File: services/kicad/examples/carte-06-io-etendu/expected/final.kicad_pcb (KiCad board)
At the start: 2 copper layers, 80 x 60 mm, 35 parts, among them J1 IN_5V, J2 SWD, J3 IO0, J4 IO1, U1 STM32F103C8T6, U2 AMS1117-3.3

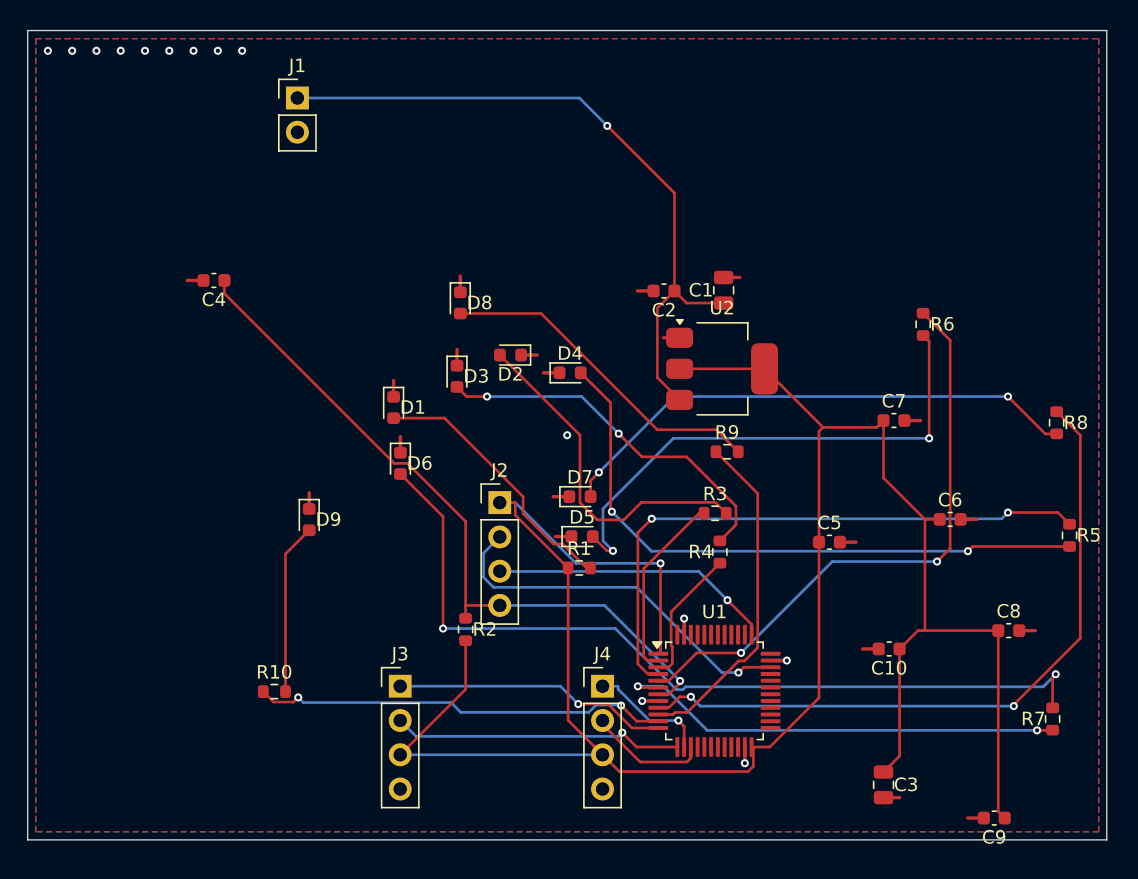
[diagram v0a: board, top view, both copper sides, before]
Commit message: feat(kicad): placement pro et routage 100 % fabricable sur les 16 cartes -- integration sur main (#164)
Branche d'integration coupee depuis origin/main (fab2a82, PR #162) : les
fichiers cles de main etaient des instantanes de feat/placement-seed-snap-
bypass (routing.py = 7981019, placement.py = 437a8b4...). On reprend donc
l'arbre entier de cette branche (345 commits, dernier 9f48667) et on y
conserve ce que main seul apportait :
- tools/verrou_routage.py + son test : « 6,2 Go par routage » rectifie
  (0,2 Go mesure ; c'est la concurrence qui emballe la memoire) ;
- tests/test_driver_llm_resync.py ;
- CLAUDE.md, PLAN.md, DECISIONS.md : fusion a trois voies, les sections
  des deux lignes conservees (2026-09-05 conteneur/verrou, 2026-09-07
  parcours asynchrone et chaine du driver, 2026-09-09/10 lecons).
Les skills *-delegate restent supprimes (remplaces le 2026-08-30).

Contenu : banc en deux phases (placement valide puis routage gele), snap
sur les regles natives, repli GND cible, journal Freerouting incremental,
horloge sans progres, via d'echappement vers le plan principal,
serigraphie degagee ; 16 cartes livrees a 100 %, 0 erreur DRC.

Verification : pytest services/kicad 1805 passed, 16 skipped ;
pnpm type-check 8/8.


Claude-Session: https://claude.ai/code/session_01TnMqm4La2CxQHHB5K8aSSV

Co-authored-by: Claude Fable 5.1 <noreply@anthropic.com>
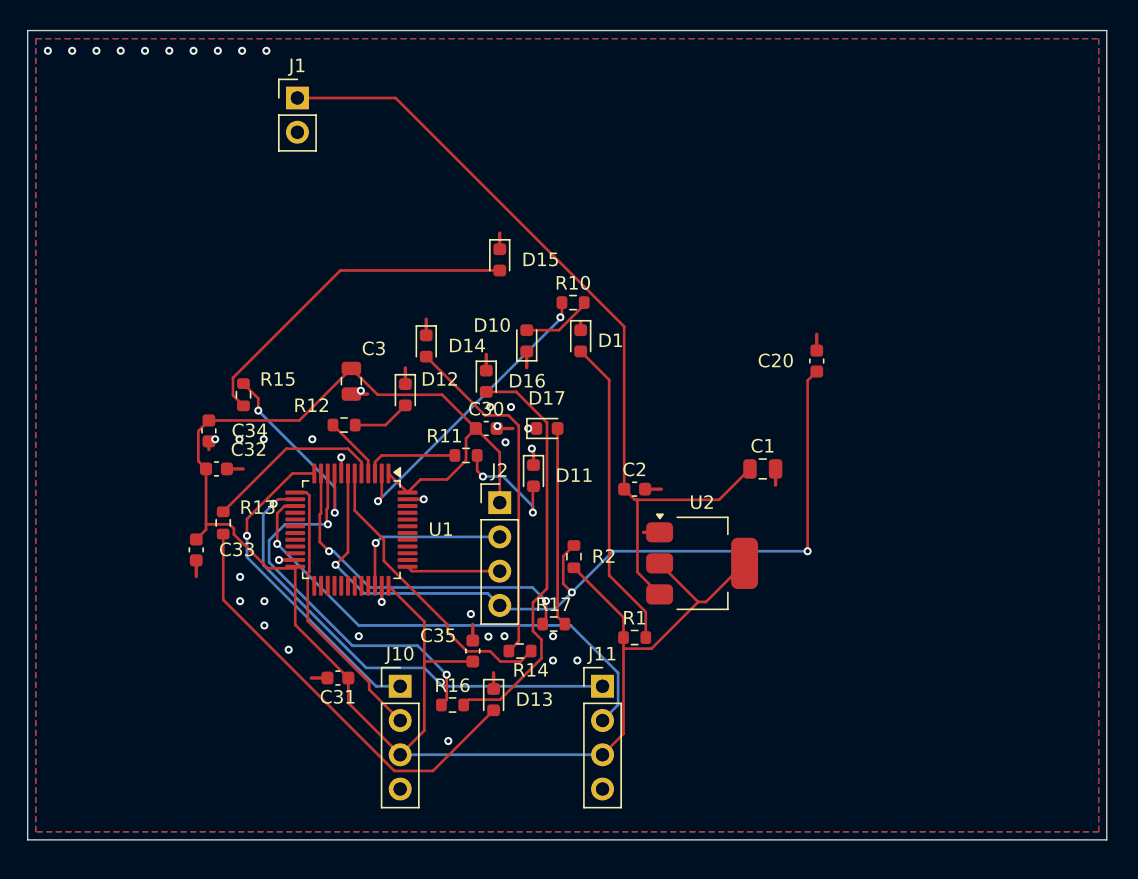
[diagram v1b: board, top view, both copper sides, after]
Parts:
- removed C10, C4, C5, C6, C7, C8, C9: 100nF, C_0603_1608Metric
- removed D2, D3, D4, D5, D6, D7, D8, D9: LED, LED_0603_1608Metric
- removed J3: IO0, PinHeader_1x04_P2.54mm_Vertical
- removed J4: IO1, PinHeader_1x04_P2.54mm_Vertical
- removed R3, R4, R5, R6, R7, R8, R9: 1k, R_0603_1608Metric
- added C20: 100nF, C_0603_1608Metric, F.Cu at (167.0, 99.5)
- added C30: 100nF, C_0603_1608Metric, F.Cu at (142.5, 104.5)
- added C31: 100nF, C_0603_1608Metric, F.Cu at (131.5, 123.0)
- added C32: 100nF, C_0603_1608Metric, F.Cu at (122.5, 107.5)
- added C33: 100nF, C_0603_1608Metric, F.Cu at (121.0, 113.5)
- added C34: 100nF, C_0603_1608Metric, F.Cu at (121.9, 104.7)
- added C35: 100nF, C_0603_1608Metric, F.Cu at (141.5, 121.0)
- added D10: LED, LED_0603_1608Metric, F.Cu at (145.5, 98.0)
- added D11: LED, LED_0603_1608Metric, F.Cu at (146.0, 108.0)
- added D12: LED, LED_0603_1608Metric, F.Cu at (136.5, 102.0)
- added D13: LED, LED_0603_1608Metric, F.Cu at (143.0, 124.6)
- added D14: LED, LED_0603_1608Metric, F.Cu at (138.0, 98.4)
- added D15: LED, LED_0603_1608Metric, F.Cu at (143.5, 92.0)
- added D16: LED, LED_0603_1608Metric, F.Cu at (142.5, 101.0)
- added D17: LED, LED_0603_1608Metric, F.Cu at (147.0, 104.5)
- added J10: IO0, PinHeader_1x04_P2.54mm_Vertical, F.Cu at (136.1, 123.6)
- added J11: IO1, PinHeader_1x04_P2.54mm_Vertical, F.Cu at (151.1, 123.6)
- added R11: 1k, R_0603_1608Metric, F.Cu at (141.0, 106.5)
- added R12: 1k, R_0603_1608Metric, F.Cu at (132.0, 104.2)
- added R13: 1k, R_0603_1608Metric, F.Cu at (123.0, 111.5)
- added R14: 1k, R_0603_1608Metric, F.Cu at (145.0, 121.0)
- added R15: 1k, R_0603_1608Metric, F.Cu at (124.5, 102.0)
- added R16: 1k, R_0603_1608Metric, F.Cu at (140.0, 125.0)
- added R17: 1k, R_0603_1608Metric, F.Cu at (147.5, 119.0)
- moved C3 49.5 mm to (132.5, 101.0)
- moved R10 36.4 mm to (148.9, 95.2)
- moved U1 29.5 mm to (132.5, 112.0), turned to -90 degrees
- moved C2 14.9 mm to (153.5, 109.0), turned to 0 degrees
- moved D1 14.7 mm to (149.5, 98.0)
- moved U2 14.5 mm to (158.5, 114.5)
- moved C1 13.6 mm to (163.0, 107.5), turned to 0 degrees
- moved R2 9.68 mm to (149.0, 114.0)
- moved R1 6.59 mm to (153.5, 120.0)
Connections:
- R10 pad 1: IO_L7 -> IO_L0
- R10 pad 2: LEDA7 -> LEDA0
- U1 pad 36: Net-(U1-36) -> +3V3
- U1 pad 48: Net-(U1-48) -> +3V3
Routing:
- net LEDA2: track 46.5 -> 4.32 mm, vias 2 -> 0
- net IO_L2: track 44.5 -> 4.67 mm, vias 2 -> 0
- net LEDA4: track 63.1 -> 26.0 mm, vias 2 -> 0
- net IO_L5: track 51.6 -> 15.3 mm
- net +3V3: track 175.2 -> 139.1 mm, vias 1 -> 0
- net IO_L3: track 44.0 -> 13.4 mm, vias 2 -> 0
- net EXT1_2: track 8.93 -> 37.1 mm, vias 0 -> 1
- net EXT1_1: track 8.94 -> 35.5 mm
- net LEDA0: track 25.6 -> 5.21 mm
- net LEDA1: track 27.4 -> 8.79 mm
- net SWDIO: track 27.9 -> 12.6 mm
- net SWCLK: track 21.1 -> 6.97 mm, vias 1 -> 0
- net LEDA5: track 39.5 -> 25.5 mm, vias 2 -> 0
- net IO_L4: track 33.7 -> 22.0 mm, vias 2 -> 0
- net VIN: track 51.4 -> 61.6 mm, vias 1 -> 0
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
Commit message: test(examples): quatre cartes livrées plus petites — contour resserré mesuré sur le banc (D-2026-09-13-c A)
Banc rejoué en taille heuristique (phase 1 puis phase 2 à placement gelé) :
carte-01 25x20 -> 24,8x17 (84 % de surface), carte-04 60x45 -> 45x44,8
(75 %), carte-06 80x60 -> 65,2x59,8 (81 %), carte-07 110x80 -> 99,5x79,8
(90 %) — toutes 100 % routées, 0 erreur DRC (vérifié en local), rendus 3D
régénérés. Gain nul sur les cartes denses (le génétique remplit la carte) ;
08 et 09 non livrées (dispersion du routage, surface inchangée) ; carte-11
non livrée (carte d'escalade). Tableau complet dans docs/DECISIONS.md.

Co-Authored-By: Claude Fable 5.1 <noreply@anthropic.com>
Claude-Session: https://claude.ai/code/session_01TnMqm4La2CxQHHB5K8aSSV
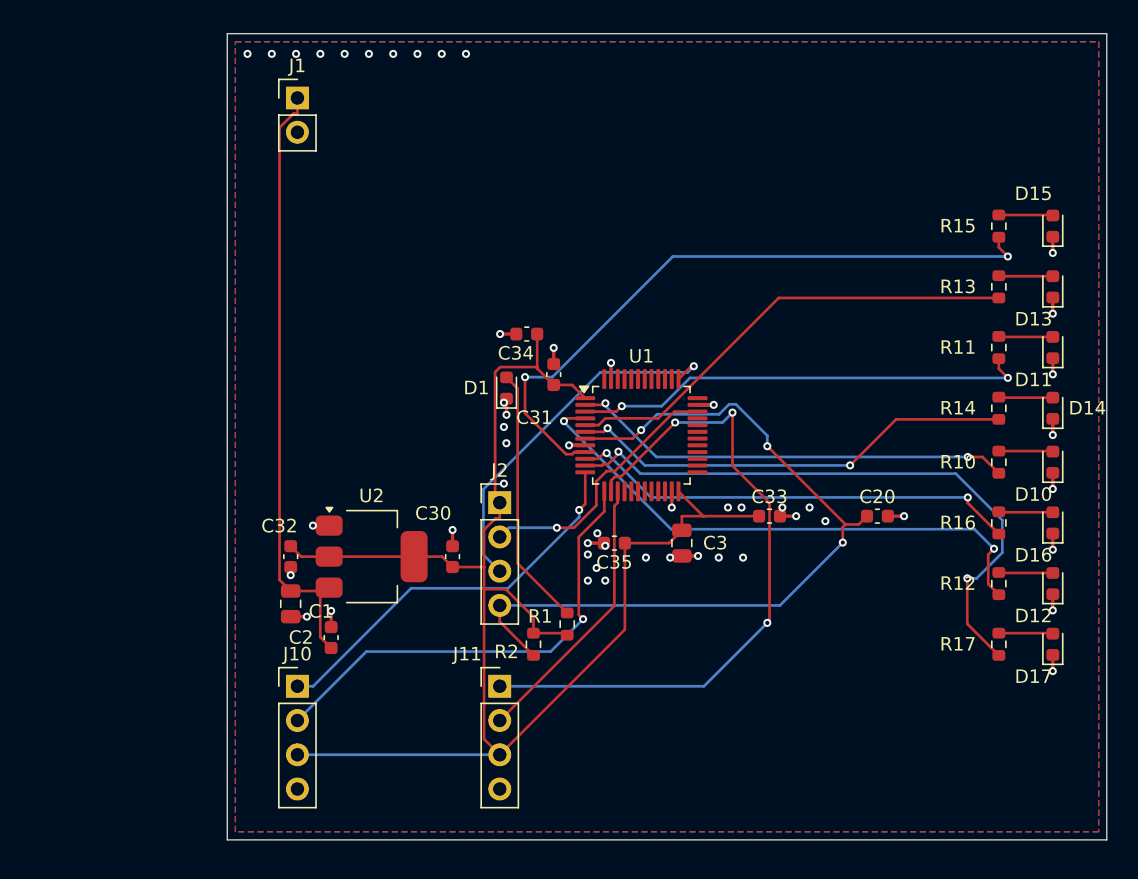
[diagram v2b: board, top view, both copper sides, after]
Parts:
- moved R13 60.1 mm to (180.5, 94.0), turned to 90 degrees
- moved R15 57.4 mm to (180.5, 89.5), turned to 90 degrees
- moved D13 51.5 mm to (184.5, 94.0), turned to 90 degrees
- moved D12 50.0 mm to (184.5, 116.0), turned to 90 degrees
- moved R12 49.9 mm to (180.5, 116.0), turned to 90 degrees
- moved D14 46.7 mm to (184.5, 103.0), turned to 90 degrees
- moved D16 43.3 mm to (184.5, 111.5), turned to 90 degrees
- moved R16 42.7 mm to (180.5, 111.5), turned to 90 degrees
- moved C33 42.6 mm to (163.5, 111.0), turned to 0 degrees
- moved D15 41.1 mm to (184.5, 89.5), turned to 90 degrees
- moved D17 40.8 mm to (184.5, 120.5), turned to 90 degrees
- moved R11 40.3 mm to (180.5, 98.5), turned to 90 degrees
- moved D10 40.0 mm to (184.5, 107.0)
- moved R14 39.8 mm to (180.5, 103.0), turned to 90 degrees
- moved D11 39.7 mm to (184.5, 98.5), turned to 90 degrees
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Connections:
- U1 pad 36: +3V3 -> Net-(U1-36)
- U1 pad 48: +3V3 -> Net-(U1-48)
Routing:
- net IO_L2: track 4.67 -> 41.4 mm, vias 0 -> 2
- net IO_L5: track 15.3 -> 49.7 mm
- net LEDA3: track 32.0 -> 4.02 mm
- net IO_L1: track 6.98 -> 34.1 mm, vias 0 -> 2
- net +3V3: track 139.1 -> 112.3 mm
- net LEDA6: track 30.8 -> 4.02 mm
- net LEDA4: track 26.0 -> 4.02 mm
- net LEDA5: track 25.5 -> 4.02 mm
- net IO_L3: track 13.4 -> 34.6 mm
- net SWCLK: track 6.97 -> 27.5 mm, vias 0 -> 1
- net IO_L7: track 25.5 -> 46.0 mm
- net VIN: track 61.6 -> 45.1 mm
- net EXT1_2: track 37.1 -> 20.6 mm, vias 1 -> 0
- net EXT1_1: track 35.5 -> 50.5 mm, vias 1 -> 3
- net EXT0_2: track 20.7 -> 34.7 mm, vias 0 -> 1
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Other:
- board size 80 x 60 mm -> 65.2 x 59.8 mm

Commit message: chore(banc): relivrer carte-01..10 avec la couture corrigee
Boards reroutes par HTTP depuis placement.kicad_pcb inchange, avec le
code de #217. Juges par remesurer_banc.py : 0 erreur, 0 connexion
manquante sur les dix. 678 -> 443 vias ; la rangee de vias GND du bord
haut a disparu.

mesures.json : `board` recompte, `drc_du_board` rejuge, nouvelle cle
`couture_corrigee` (date, vias_avant, couches). journal.txt et les
champs du run d origine sont laisses tels quels et le disent.
rendu-3d.png : kicad-cli, modeles 3D, iso 1400x900.

Couches d un tirage : huit cartes sur 2, carte-08 et carte-10 sur 4.
CLAUDE.md et BANC_DRIVER_LLM.md recomptes. carte-11 non touchee.

Co-Authored-By: Claude Opus 5 (1M context) <noreply@anthropic.com>
Claude-Session: https://claude.ai/code/session_01TnMqm4La2CxQHHB5K8aSSV
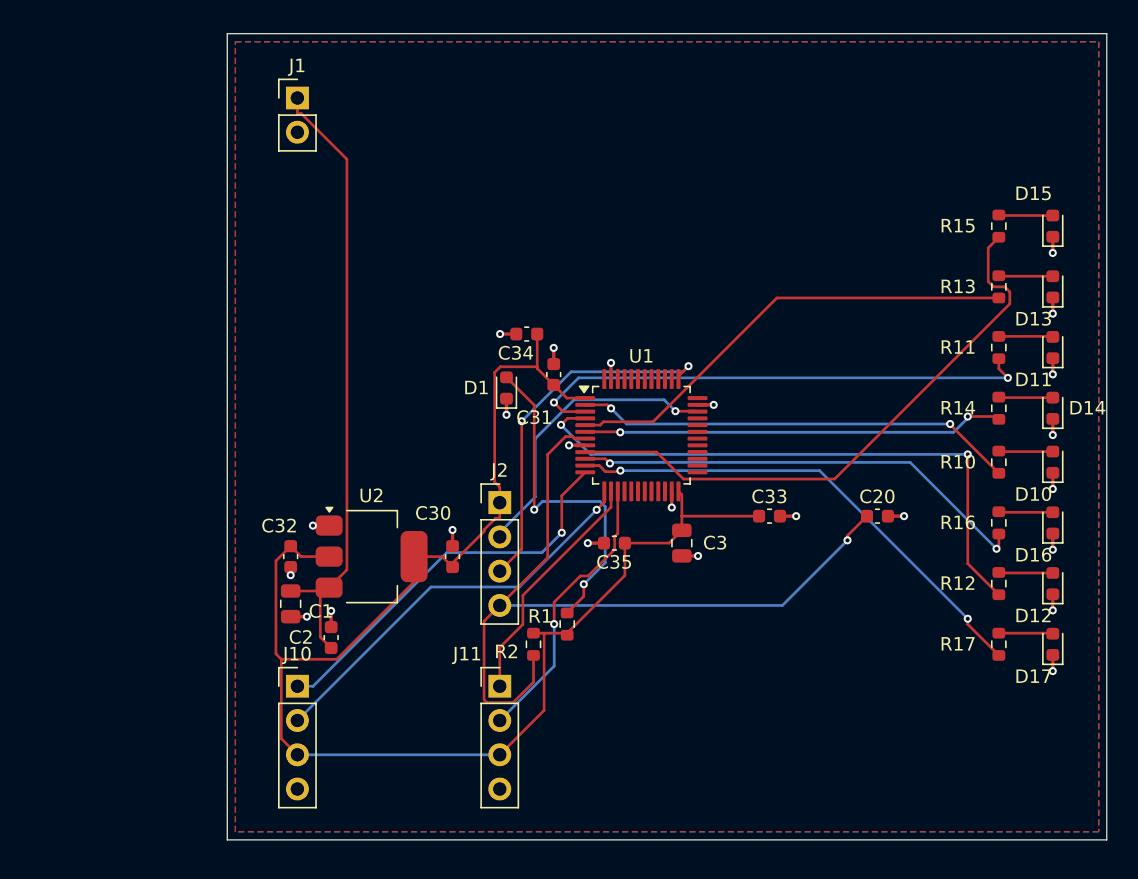
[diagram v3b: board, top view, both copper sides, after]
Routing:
- net EXT1_1: track 50.5 -> 17.9 mm, vias 3 -> 0
- net IO_L7: track 46.0 -> 36.8 mm
- net LED_PWR: track 19.3 -> 25.4 mm, vias 0 -> 2
- net IO_L5: track 49.7 -> 44.1 mm, vias 2 -> 0
- net IO_L1: track 34.1 -> 38.7 mm
- net EXT0_2: track 34.7 -> 30.3 mm
- net IO_L2: track 41.4 -> 44.4 mm
- net SWDIO: track 19.6 -> 22.0 mm
- net GND: track 30.6 -> 28.2 mm, vias 53 -> 24
- net IO_L4: track 33.3 -> 31.3 mm
- net +3V3: track 112.3 -> 113.3 mm
- net VIN: track 45.1 -> 46.0 mm
- net IO_L6: track 33.6 -> 34.5 mm
- net SWCLK: track 27.5 -> 27.1 mm, vias 1 -> 2
- net EXT1_2: track 20.6 -> 20.9 mm, vias 0 -> 1
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
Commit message: chore(banc): relivrer carte-03 et carte-06 compactes apres le correctif des angles
Rejeu complet place -> route des dix cartes par HTTP, code de #223/#224.

  carte-03  50 x 35     -> 27,8 x 19,8   0 erreur · 0 manquante
            (12 erreurs · 9 manquantes le matin, avant #224)
  carte-06  65,2 x 59,8 -> 48,4 x 36,3   0 erreur · 0 manquante

placement.kicad_pcb et final.kicad_pcb remplaces ensemble ; mesures.json
recompte et rejuge (remesurer_banc.py), cle carte_compacte ; rendus refaits.

Tableau des dix cartes dans BANC_DRIVER_LLM.md. 01/02/04/05 gardent leur
board compact du 20/09 matin (propres). 05 et 09 sortent a 1 erreur
(courtyards_overlap U2 <-> passif voisin), 07/08/10 routent desormais mais
gardent 10 a 18 connexions manquantes : non relivrees.

Co-Authored-By: Claude Fable 5.1 <noreply@anthropic.com>
Claude-Session: https://claude.ai/code/session_01TnMqm4La2CxQHHB5K8aSSV
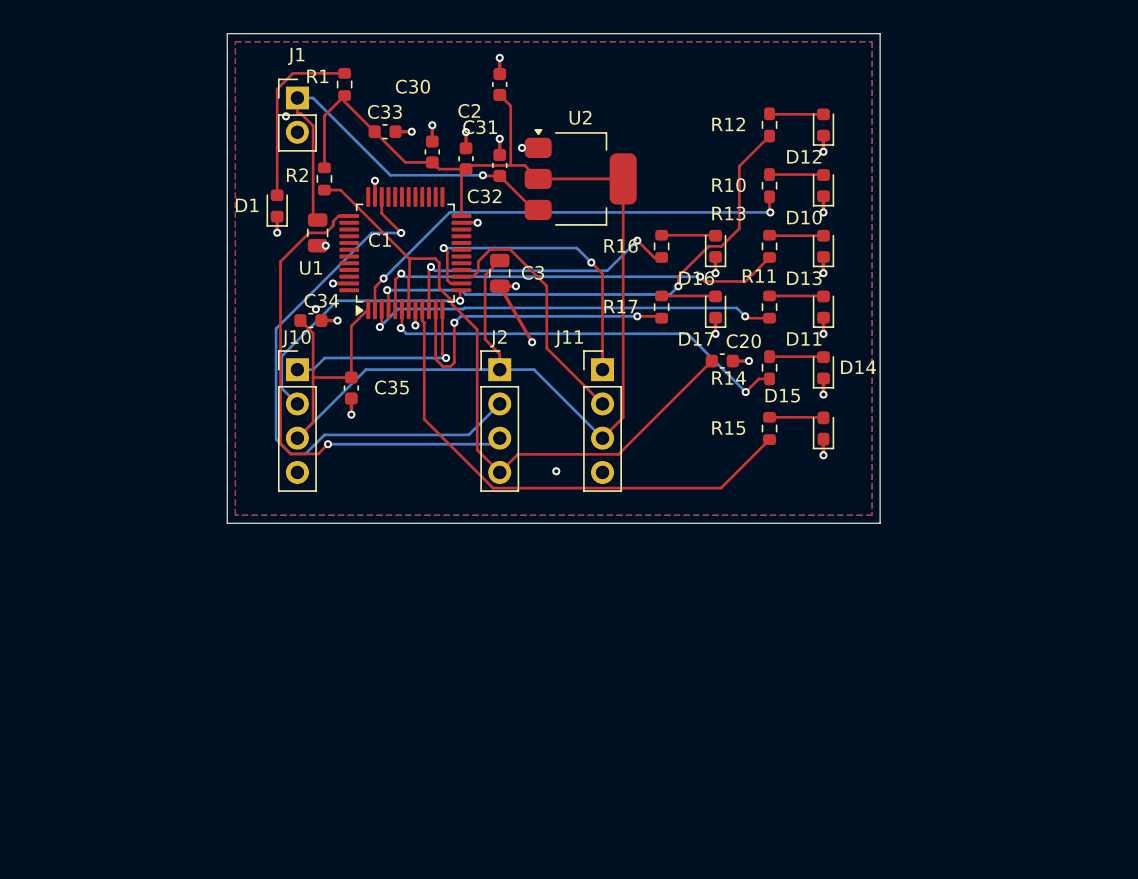
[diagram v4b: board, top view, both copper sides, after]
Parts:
- moved R1 43.3 mm to (132.0, 79.0)
- moved C33 40.3 mm to (135.0, 82.5)
- moved D12 38.0 mm to (167.5, 82.0)
- moved R12 38.0 mm to (163.5, 82.0)
- moved R2 37.8 mm to (130.5, 86.0)
- moved C2 37.2 mm to (143.5, 85.0)
- moved D17 35.4 mm to (159.5, 95.5)
- moved R17 35.4 mm to (155.5, 95.5)
- moved D16 32.3 mm to (159.5, 91.0)
- moved R16 32.3 mm to (155.5, 91.0)
- moved C32 32.2 mm to (141.0, 84.5), turned to 90 degrees
- moved U2 32.0 mm to (149.5, 86.0)
- moved C30 30.0 mm to (138.5, 84.0)
- moved C1 27.6 mm to (130.0, 90.0)
- moved D10 26.6 mm to (167.5, 86.5)
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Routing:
- net SWDIO: track 22.0 -> 42.3 mm
- net VIN: track 46.0 -> 31.1 mm, vias 0 -> 1
- net EXT0_1: track 29.5 -> 15.1 mm
- net IO_L7: track 36.8 -> 24.0 mm
- net IO_L6: track 34.5 -> 21.9 mm
- net LED_PWR: track 25.4 -> 13.4 mm, vias 2 -> 0
- net EXT0_2: track 30.3 -> 19.8 mm
- net SWCLK: track 27.1 -> 37.2 mm, vias 2 -> 1
- net NRST: track 60.1 -> 51.1 mm, vias 1 -> 0
- net IO_L1: track 38.7 -> 31.2 mm
- net IO_L5: track 44.1 -> 37.4 mm
- net IO_L2: track 44.4 -> 37.9 mm
- net EXT1_1: track 17.9 -> 23.3 mm, vias 0 -> 2
- net GND: track 28.2 -> 33.0 mm, vias 24 -> 28
- net IO_L3: track 34.6 -> 31.1 mm, vias 0 -> 2
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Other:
- board size 65.2 x 59.8 mm -> 48.4 x 36.3 mm
